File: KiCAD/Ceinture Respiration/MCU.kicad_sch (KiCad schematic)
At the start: 3 parts

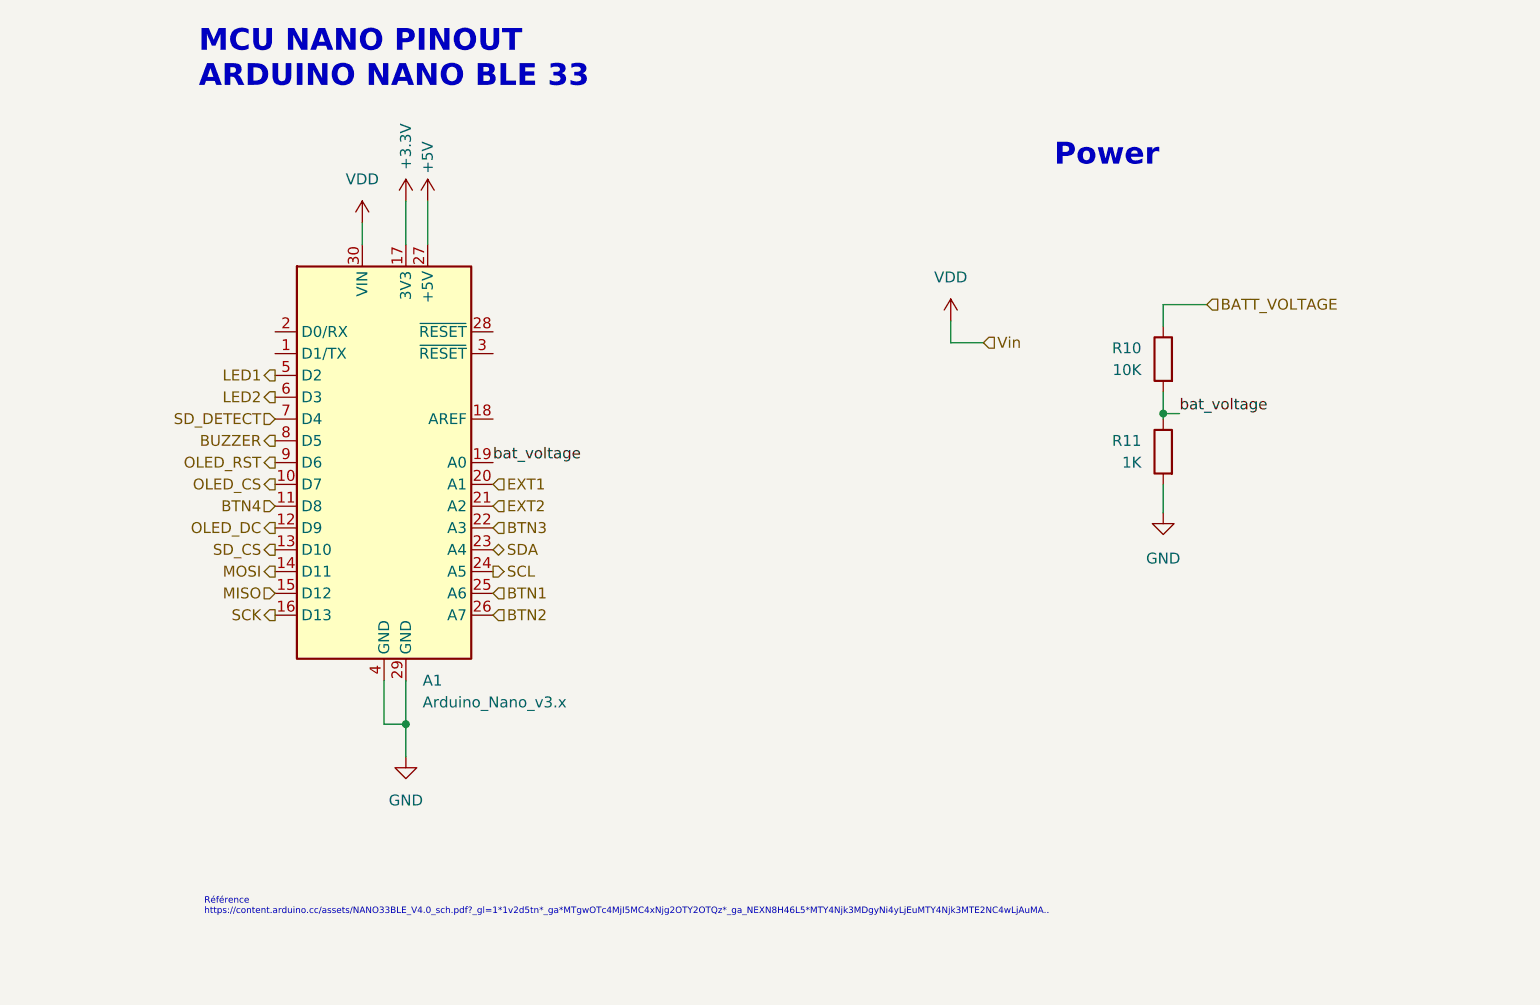
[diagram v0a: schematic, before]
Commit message: Schematique 99%, PCB 50%
schématique complété, nettoyé et layout complété, reste routage
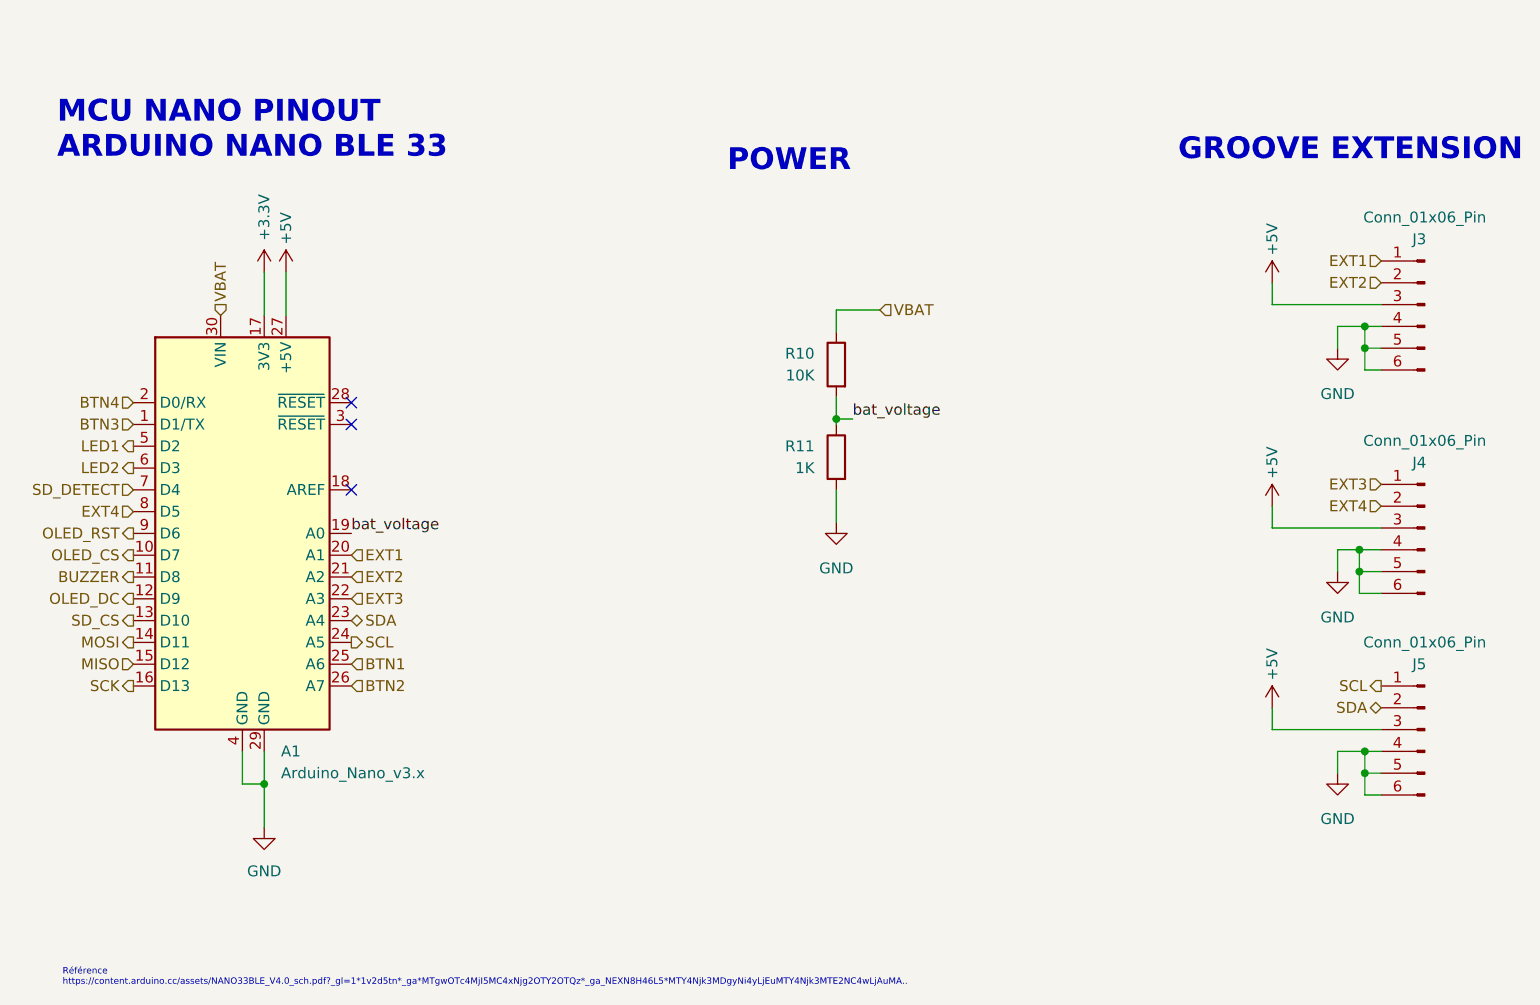
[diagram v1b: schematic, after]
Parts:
- added J3, J4, J5: Conn_01x06_Pin, CentureResp:CONN4_20164_SEE, symbol Connector:Conn_01x06_Pin
- A1: footprint Module:Arduino_Nano -> CentureResp:MODULE_ABX00027
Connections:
- net VDD is gone; now on net VBAT: A1.30 (VIN)
- net +5V: now also J3.3 (Pin_3), J4.3 (Pin_3), J5.3 (Pin_3)
- net BTN3: now also A1.1 (D1/TX); no longer A1.22 (A3)
- net BTN4: now also A1.2 (D0/RX); no longer A1.11 (D8)
- net BUZZER: now also A1.11 (D8); no longer A1.8 (D5)
- net EXT1: now also J3.1 (Pin_1)
- net EXT2: now also J3.2 (Pin_2)
- net GND: now also J3.4 (Pin_4), J3.5 (Pin_5), J3.6 (Pin_6), J4.4 (Pin_4), J4.5 (Pin_5), J4.6 (Pin_6), J5.4 (Pin_4), J5.5 (Pin_5), J5.6 (Pin_6)
- net SCL: now also J5.1 (Pin_1)
- net SDA: now also J5.2 (Pin_2)
- net BATT_VOLTAGE renamed VBAT
- new net EXT3: A1.22 (A3), J4.1 (Pin_1)
- new net EXT4: A1.8 (D5), J4.2 (Pin_2)
- no-connect marks 0 -> 3
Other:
- note added: "GROOVE EXTENSION"
- note added: "POWER"
- note removed: "Power"
- company: (none) -> IngRéadapt UL
- moved on the sheet: A1, R10, R11

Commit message: sch 99% pcb 99%
Reste à préparer les commandes
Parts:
- added R10 (x2): 10K, Resistor_SMD:R_0603_1608Metric, symbol Device:R
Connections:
- net +3.3V: now also R10.1, R10.1
- net SCL: now also R10.2
- net SDA: now also R10.2
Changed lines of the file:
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@@
   (junction (at 215.265 107.95) (diameter 0) (color 0 0 0 0)
+  )
+  (junction (at 151.13 128.905) (diameter 0) (color 0 0 0 0)
   )
   (no_connect (at 97.79 100.965))
@@
     (stroke (width 0) (type default))
   )
+  (wire (pts (xy 159.385 138.43) (xy 159.385 142.24))
+    (stroke (width 0) (type default))
+  )
   (wire (pts (xy 215.9 84.455) (xy 217.805 84.455))
     (stroke (width 0) (type default))
@@
     (stroke (width 0) (type default))
   )
+  (wire (pts (xy 151.13 138.43) (xy 151.13 142.24))
+    (stroke (width 0) (type default))
+  )
   (wire (pts (xy 212.725 81.915) (xy 215.9 81.915))
     (stroke (width 0) (type default))
@@
     (stroke (width 0) (type default))
   )
+  (wire (pts (xy 159.385 128.905) (xy 151.13 128.905))
+    (stroke (width 0) (type default))
+  )
   (wire (pts (xy 215.265 107.95) (xy 217.805 107.95))
     (stroke (width 0) (type default))
@@
     (stroke (width 0) (type default))
   )
+  (wire (pts (xy 151.13 126.365) (xy 151.13 128.905))
+    (stroke (width 0) (type default))
+  )
   (wire (pts (xy 217.805 136.525) (xy 215.9 136.525))
     (stroke (width 0) (type default))
   )
+  (wire (pts (xy 159.385 130.81) (xy 159.385 128.905))
+    (stroke (width 0) (type default))
+  )
   (wire (pts (xy 212.725 131.445) (xy 215.9 131.445))
     (stroke (width 0) (type default))
@@
   )
   (wire (pts (xy 217.805 86.995) (xy 215.9 86.995))
+    (stroke (width 0) (type default))
+  )
+  (wire (pts (xy 151.13 128.905) (xy 151.13 130.81))
     (stroke (width 0) (type default))
   )
@@
     (effects (font (size 1.27 1.27)) (justify right))
   )
+  (hierarchical_label "SDA" (shape bidirectional) (at 159.385 142.24 270) (fields_autoplaced)
+    (effects (font (size 1.27 1.27)) (justify right))
+  )
   (hierarchical_label "EXT2" (shape input) (at 217.805 76.835 180) (fields_autoplaced)
     (effects (font (size 1.27 1.27)) (justify right))
@@
   )
   (hierarchical_label "SDA" (shape bidirectional) (at 217.805 126.365 180) (fields_autoplaced)
+    (effects (font (size 1.27 1.27)) (justify right))
+  )
+  (hierarchical_label "SCL" (shape output) (at 151.13 142.24 270) (fields_autoplaced)
     (effects (font (size 1.27 1.27)) (justify right))
   )
@@
     )
   )
+  (symbol (lib_id "Device:R") (at 159.385 134.62 0) (mirror y) (unit 1)
+    (in_bom yes) (on_board yes) (dnp no) (fields_autoplaced)
+    (property "Reference" "R10" (at 156.845 133.35 0)
+      (effects (font (size 1.27 1.27)) (justify left))
+    )
+    (property "Value" "10K" (at 156.845 135.89 0)
+      (effects (font (size 1.27 1.27)) (justify left))
+    )
+    (property "Footprint" "Resistor_SMD:R_0603_1608Metric" (at 161.163 134.62 90)
+      (effects (font (size 1.27 1.27)) hide)
+    )
+    (property "Datasheet" "~" (at 159.385 134.62 0)
+      (effects (font (size 1.27 1.27)) hide)
+    )
+    (pin "1")
+    (pin "2")
+    (instances
+      (project "Ceinture Respiration"
+        (path "/5bd6870d-598f-44db-8dd6-81ffc3a9b2d4"
+          (reference "R10") (unit 1)
+        )
+        (path "/5bd6870d-598f-44db-8dd6-81ffc3a9b2d4/c778e6e5-e4c6-4658-8d5f-7ddd15204d0f"
+          (reference "R11") (unit 1)
+        )
+      )
+    )
+  )
   (symbol (lib_id "power:+5V") (at 90.17 75.565 0) (unit 1)
     (in_bom yes) (on_board yes) (dnp no)
@@
     )
   )
+  (symbol (lib_id "Device:R") (at 151.13 134.62 0) (mirror y) (unit 1)
+    (in_bom yes) (on_board yes) (dnp no) (fields_autoplaced)
+    (property "Reference" "R10" (at 148.59 133.35 0)
+      (effects (font (size 1.27 1.27)) (justify left))
+    )
+    (property "Value" "10K" (at 148.59 135.89 0)
+      (effects (font (size 1.27 1.27)) (justify left))
+    )
+    (property "Footprint" "Resistor_SMD:R_0603_1608Metric" (at 152.908 134.62 90)
+      (effects (font (size 1.27 1.27)) hide)
+    )
+    (property "Datasheet" "~" (at 151.13 134.62 0)
+      (effects (font (size 1.27 1.27)) hide)
+    )
+    (pin "1")
+    (pin "2")
+    (instances
+      (project "Ceinture Respiration"
+        (path "/5bd6870d-598f-44db-8dd6-81ffc3a9b2d4"
+          (reference "R10") (unit 1)
+        )
+        (path "/5bd6870d-598f-44db-8dd6-81ffc3a9b2d4/c778e6e5-e4c6-4658-8d5f-7ddd15204d0f"
+          (reference "R10") (unit 1)
+        )
+      )
+    )
+  )
   (symbol (lib_id "power:+5V") (at 205.105 76.835 0) (mirror y) (unit 1)
     (in_bom yes) (on_board yes) (dnp no)
@@
         )
       )
+    )
+  )
+  (symbol (lib_id "power:+3.3V") (at 151.13 126.365 0) (unit 1)
+    (in_bom yes) (on_board yes) (dnp no)
+    (property "Reference" "#PWR010" (at 151.13 130.175 0)
+      (effects (font (size 1.27 1.27)) hide)
+    )
+    (property "Value" "+3.3V" (at 151.13 120.015 90)
+      (effects (font (size 1.27 1.27)))
+    )
+    (property "Footprint" "" (at 151.13 126.365 0)
+      (effects (font (size 1.27 1.27)) hide)
+    )
+    (property "Datasheet" "" (at 151.13 126.365 0)
+      (effects (font (size 1.27 1.27)) hide)
+    )
+    (pin "1")
+    (instances
+      (project "Ceinture Respiration"
+        (path "/5bd6870d-598f-44db-8dd6-81ffc3a9b2d4"
+          (reference "#PWR010") (unit 1)
+        )
+        (path "/5bd6870d-598f-44db-8dd6-81ffc3a9b2d4/c778e6e5-e4c6-4658-8d5f-7ddd15204d0f"
+          (reference "#PWR041") (unit 1)
+        )
+      )

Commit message: PCB sent for production
See latest production files.
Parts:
- R10: LCSC (none) -> C25804
- R11: LCSC (none) -> C21190
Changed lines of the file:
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@@
+      (effects (font (size 1.27 1.27)) hide)
+    )
+    (property "LCSC" "C21190" (at 154.305 97.155 0)
       (effects (font (size 1.27 1.27)) hide)
     )
@@
       (effects (font (size 1.27 1.27)) hide)
     )
+    (property "LCSC" "C25804" (at 159.385 134.62 0)
+      (effects (font (size 1.27 1.27)) hide)
+    )
     (pin "1")
     (pin "2")
@@
       (effects (font (size 1.27 1.27)) hide)
     )
+    (property "LCSC" "C25804" (at 151.13 134.62 0)
+      (effects (font (size 1.27 1.27)) hide)
+    )
     (pin "1")
     (pin "2")
@@
       (effects (font (size 1.27 1.27)) hide)
     )
+    (property "LCSC" "C25804" (at 154.305 86.36 0)
+      (effects (font (size 1.27 1.27)) hide)
+    )
